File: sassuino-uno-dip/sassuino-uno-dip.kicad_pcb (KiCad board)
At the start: 2 copper layers, 68.6 x 53.3 mm, 30 parts, among them J1 USB_B, J10 OSCPWR_HDR, J2 POWER2_HDR, J3 ICSP_HDR, J4 POWER_HDR, J5 PORTC_HDR, J6 PORTB_HDR, J7 PORTD_HDR, J8 XTAL2_HDR, J9 XTAL1_HDR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

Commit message: Add the actual footprint/model of the pushbutton switch I'm using.
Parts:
- SW1: footprint Button_Switch_THT:SW_PUSH_6mm -> 0SassuinoFP:SW4_1825910-B_TEC
- moved SW1 7.80 mm to (57.8, 146.0)
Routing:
- net /~{RESET}: track 110.8 -> 107.2 mm
- net GND: vias 38 -> 37

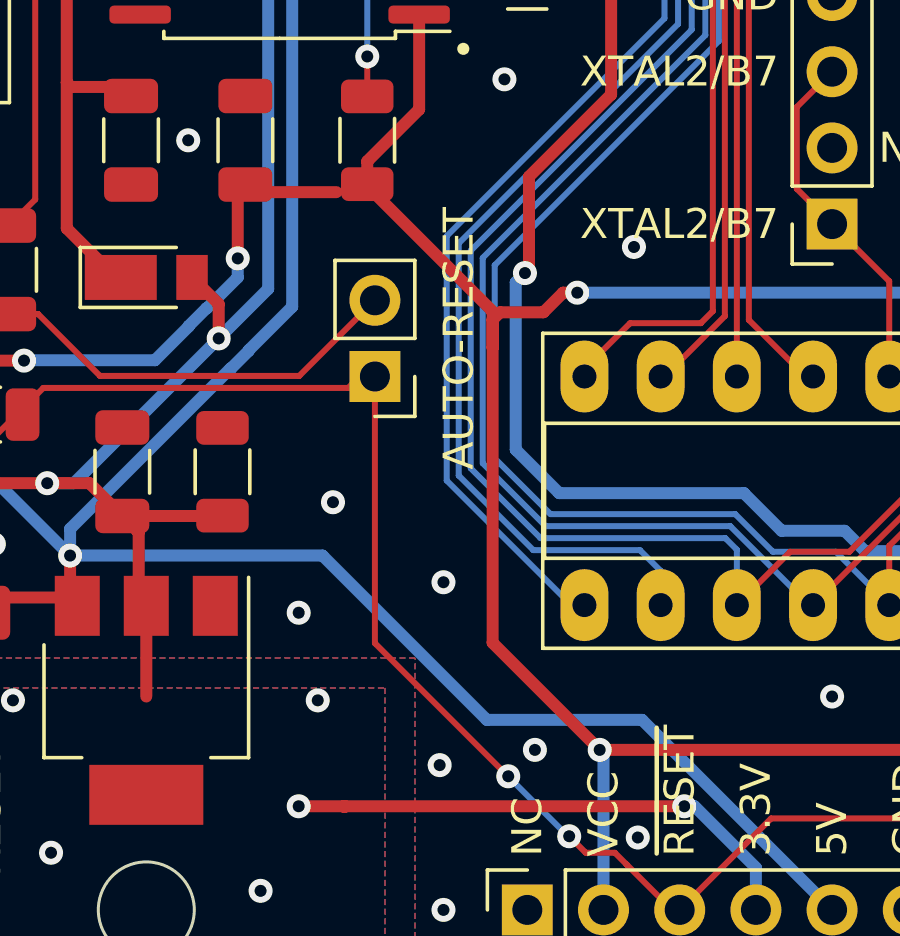
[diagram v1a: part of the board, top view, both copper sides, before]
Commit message: Add a clamp diode to the reset circuit.
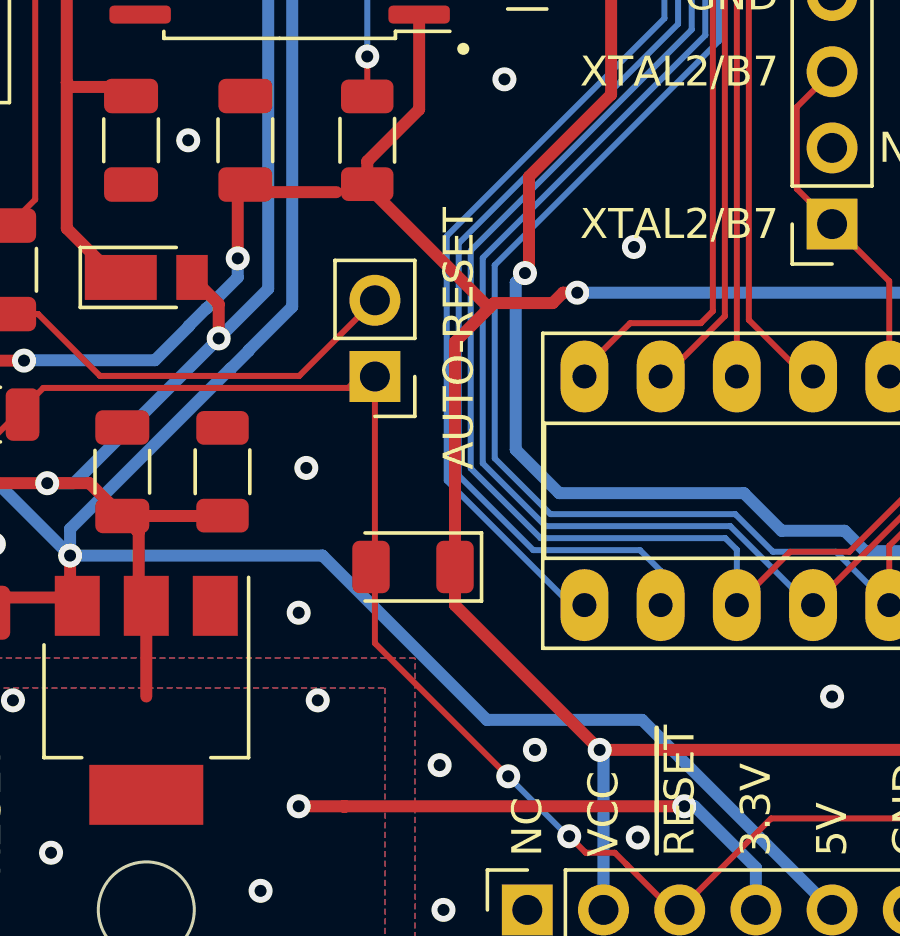
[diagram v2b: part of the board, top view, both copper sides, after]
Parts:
- added D2: TS4148 RAG, Diode_SMD:D_1206_3216Metric, F.Cu at (74.9, 141.0)
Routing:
- net GND: vias 37 -> 36
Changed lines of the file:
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@@
+    )
+  )
+  (footprint "Diode_SMD:D_1206_3216Metric" (layer "F.Cu")
+    (at 74.93 140.97 180)
+    (descr "Diode SMD 1206 (3216 Metric), square (rectangular) end terminal, IPC_7351 nominal, (Body size source: http://www.tortai-tech.com/upload/download/2011102023233369053.pdf), generated with kicad-footprint-generator")
+    (tags "diode")
+    (property "Sheetfile" "sassuino-uno-dip.kicad_sch")
+    (property "Sheetname" "")
+    (attr smd)
+    (fp_text reference "D2" (at 0 -1.82) (layer "F.SilkS") hide
+      (effects (font (size 1 1) (thickness 0.15)))
+    )
+    (fp_text value "TS4148 RAG" (at 0 1.82) (layer "F.Fab")
+      (effects (font (size 1 1) (thickness 0.15)))
+    )
+    (fp_text user "${REFERENCE}" (at 0 0) (layer "F.Fab")
+      (effects (font (size 0.8 0.8) (thickness 0.12)))
+    )
+    (fp_line (start -2.285 -1.135) (end -2.285 1.135) (layer "F.SilkS") (width 0.12))
+    (fp_line (start 1.6 -1.135) (end -2.285 -1.135) (layer "F.SilkS") (width 0.12))
+    (fp_line (start -2.285 1.135) (end 1.6 1.135) (layer "F.SilkS") (width 0.12))
+    (fp_line (start -2.28 -1.12) (end 2.28 -1.12) (layer "F.CrtYd") (width 0.05))
+    (fp_line (start 2.28 -1.12) (end 2.28 1.12) (layer "F.CrtYd") (width 0.05))
+    (fp_line (start 2.28 1.12) (end -2.28 1.12) (layer "F.CrtYd") (width 0.05))
+    (fp_line (start -2.28 1.12) (end -2.28 -1.12) (layer "F.CrtYd") (width 0.05))
+    (fp_line (start -1.6 -0.4) (end -1.6 0.8) (layer "F.Fab") (width 0.1))
+    (fp_line (start 1.6 -0.8) (end -1.2 -0.8) (layer "F.Fab") (width 0.1))
+    (fp_line (start -1.6 0.8) (end 1.6 0.8) (layer "F.Fab") (width 0.1))
+    (fp_line (start 1.6 0.8) (end 1.6 -0.8) (layer "F.Fab") (width 0.1))
+    (fp_line (start -1.2 -0.8) (end -1.6 -0.4) (layer "F.Fab") (width 0.1))
+    (pad "1" smd roundrect (at -1.4 0 180) (size 1.25 1.75) (layers "F.Cu" "F.Paste" "F.Mask") (roundrect_rratio 0.2)
+      (net 29 "VCC") (pinfunction "K") (pintype "passive"))
+    (pad "2" smd roundrect (at 1.4 0 180) (size 1.25 1.75) (layers "F.Cu" "F.Paste" "F.Mask") (roundrect_rratio 0.2)
+      (net 8 "/~{RESET}") (pinfunction "A") (pintype "passive"))
+    (model "${KICAD6_3DMODEL_DIR}/Diode_SMD.3dshapes/D_1206_3216Metric.wrl"
+      (offset (xyz 0 0 0))
+      (scale (xyz 1 1 1))
+      (rotate (xyz 0 0 0))
     )
   )
@@
   (via (at 96.52 112.776) (size 0.8) (drill 0.4) (layers "F.Cu" "B.Cu") (free) (net 2))
   (via (at 85.852 110.8275) (size 0.8) (drill 0.4) (layers "F.Cu" "B.Cu") (free) (net 2))
-  (via (at 72.263 138.811) (size 0.8) (drill 0.4) (layers "F.Cu" "B.Cu") (free) (net 2))
+  (via (at 71.374 137.668) (size 0.8) (drill 0.4) (layers "F.Cu" "B.Cu") (free) (net 2))
   (via (at 102.87 131.318) (size 0.8) (drill 0.4) (layers "F.Cu" "B.Cu") (free) (net 2))
   (via (at 67.437 126.746) (size 0.8) (drill 0.4) (layers "F.Cu" "B.Cu") (free) (net 2))
@@
   (via (at 62.484 107.95) (size 0.8) (drill 0.4) (layers "F.Cu" "B.Cu") (free) (net 2))
   (via (at 58.42 132.588) (size 0.8) (drill 0.4) (layers "F.Cu" "B.Cu") (free) (net 2))
-  (via (at 75.946 141.478) (size 0.8) (drill 0.4) (layers "F.Cu" "B.Cu") (free) (net 2))
   (via (at 110.744 131.826) (size 0.8) (drill 0.4) (layers "F.Cu" "B.Cu") (free) (net 2))
   (via (at 98.679 145.161) (size 0.8) (drill 0.4) (layers "F.Cu" "B.Cu") (free) (net 2))
@@
   (segment (start 86.474352 113.315127) (end 86.088977 113.315127) (width 0.2) (layer "B.Cu") (net 7))
   (segment (start 116.4965 135.89) (end 115.2265 134.62) (width 0.2) (layer "F.Cu") (net 8))
-  (segment (start 78.0961 147.9461) (end 73.66 143.51) (width 0.2) (layer "F.Cu") (net 8))
   (segment (start 86.868 149.352) (end 83.82 152.4) (width 0.2) (layer "F.Cu") (net 8))
-  (segment (start 73.66 143.51) (end 73.66 134.62) (width 0.2) (layer "F.Cu") (net 8))
   (segment (start 72.771 135.001) (end 73.406 134.366) (width 0.2) (layer "F.Cu") (net 8))
   (segment (start 56.642 144.702) (end 56.642 140.967207) (width 0.2) (layer "F.Cu") (net 8))
   (segment (start 82.053 150.887) (end 83.566 152.4) (width 0.2) (layer "F.Cu") (net 8))
   (segment (start 115.2265 134.62) (end 113.665 134.62) (width 0.2) (layer "F.Cu") (net 8))
+  (segment (start 73.66 143.51) (end 73.66 134.62) (width 0.2) (layer "F.Cu") (net 8))
   (segment (start 57.84 145.9) (end 56.642 144.702) (width 0.2) (layer "F.Cu") (net 8))
-  (segment (start 78.105 147.9461) (end 78.0961 147.9461) (width 0.2) (layer "F.Cu") (net 8))
   (segment (start 80.137 149.9451) (end 80.6869 150.495) (width 0.2) (layer "F.Cu") (net 8))
   (segment (start 97.028 149.352) (end 86.868 149.352) (width 0.2) (layer "F.Cu") (net 8))
@@
   (segment (start 57.7596 145.975) (end 53.259599 145.975) (width 0.2) (layer "F.Cu") (net 8))
   (segment (start 80.6869 150.495) (end 81.658207 150.495) (width 0.2) (layer "F.Cu") (net 8))
+  (segment (start 78.105 147.9461) (end 78.0961 147.9461) (width 0.2) (layer "F.Cu") (net 8))
   (segment (start 99.314 147.066) (end 97.028 149.352) (width 0.2) (layer "F.Cu") (net 8))
   (segment (start 82.050207 150.887) (end 82.053 150.887) (width 0.2) (layer "F.Cu") (net 8))
   (segment (start 81.658207 150.495) (end 82.050207 150.887) (width 0.2) (layer "F.Cu") (net 8))
   (segment (start 56.642 140.967207) (end 62.608207 135.001) (width 0.2) (layer "F.Cu") (net 8))
+  (segment (start 78.0961 147.9461) (end 73.66 143.51) (width 0.2) (layer "F.Cu") (net 8))
   (via (at 116.4965 135.89) (size 0.8) (drill 0.4) (layers "F.Cu" "B.Cu") (net 8))
   (via (at 78.105 147.9461) (size 0.8) (drill 0.4) (layers "F.Cu" "B.Cu") (net 8))
@@
   (segment (start 107.95 111.506) (end 106.372 109.928) (width 0.2) (layer "B.Cu") (net 28))
   (segment (start 75.135 125.7175) (end 75.135 122.555) (width 0.4) (layer "F.Cu") (net 29))
-  (segment (start 73.406 128.27) (end 77.5837 132.4477) (width 0.4) (layer "F.Cu") (net 29))
-  (segment (start 77.5837 133.6562) (end 77.5837 143.4967) (width 0.4) (layer "F.Cu") (net 29))
+  (segment (start 73.406 128.2085) (end 73.406 128.27) (width 0.4) (layer "F.Cu") (net 29))
   (segment (start 116.264081 122.682) (end 113.157 122.682) (width 0.4) (layer "F.Cu") (net 29))
+  (segment (start 79.931817 131.826) (end 79.58542 132.172397) (width 0.4) (layer "F.Cu") (net 29))
+  (segment (start 73.406 128.27) (end 77.47 132.334) (width 0.4) (layer "F.Cu") (net 29))
   (segment (start 73.406 128.2085) (end 73.406 127.4465) (width 0.4) (layer "F.Cu") (net 29))
   (segment (start 93.648 146.05) (end 93.648 142.543) (width 0.4) (layer "F.Cu") (net 29))
+  (segment (start 80.405767 131.826) (end 79.931817 131.826) (width 0.4) (layer "F.Cu") (net 29))
   (segment (start 97.91 130.507) (end 97.91 127.071) (width 0.4) (layer "F.Cu") (net 29))
   (segment (start 81.153 147.066) (end 92.632 147.066) (width 0.4) (layer "F.Cu") (net 29))
   (segment (start 92.632 147.066) (end 93.648 146.05) (width 0.4) (layer "F.Cu") (net 29))
-  (segment (start 77.5837 132.7283) (end 77.5837 133.6562) (width 0.4) (layer "F.Cu") (net 29))
   (segment (start 112.522 123.317) (end 112.522 126.161704) (width 0.4) (layer "F.Cu") (net 29))
-  (segment (start 77.5837 143.4967) (end 81.153 147.066) (width 0.4) (layer "F.Cu") (net 29))
   (segment (start 97.91 131.826) (end 97.91 130.507) (width 0.4) (layer "F.Cu") (net 29))
   (segment (start 57.7195 137.16) (end 53.93 137.16) (width 0.4) (layer "F.Cu") (net 29))
+  (segment (start 79.58542 132.172397) (end 77.631603 132.172397) (width 0.4) (layer "F.Cu") (net 29))
   (segment (start 97.91 130.507) (end 97.91 134.105) (width 0.4) (layer "F.Cu") (net 29))
-  (segment (start 79.931817 131.826) (end 79.277817 132.48) (width 0.4) (layer "F.Cu") (net 29))
   (segment (start 69.596 128.475) (end 72.3775 128.475) (width 0.4) (layer "F.Cu") (net 29))
-  (segment (start 77.5837 132.4477) (end 77.5837 133.6562) (width 0.4) (layer "F.Cu") (net 29))
   (segment (start 116.84 123.257919) (end 116.264081 122.682) (width 0.4) (layer "F.Cu") (net 29))
   (segment (start 69.342 128.221) (end 69.596 128.475) (width 0.4) (layer "F.Cu") (net 29))
   (segment (start 112.522 126.161704) (end 109.22 129.463704) (width 0.4) (layer "F.Cu") (net 29))
+  (segment (start 77.47 132.334) (end 76.33 133.474) (width 0.4) (layer "F.Cu") (net 29))
   (segment (start 69.088 130.683) (end 69.088 128.729) (width 0.4) (layer "F.Cu") (net 29))
-  (segment (start 80.405767 131.826) (end 79.931817 131.826) (width 0.4) (layer "F.Cu") (net 29))
   (segment (start 61.963481 134.090568) (end 60.788932 134.090568) (width 0.4) (layer "F.Cu") (net 29))
   (segment (start 58.9895 135.89) (end 57.7195 137.16) (width 0.4) (layer "F.Cu") (net 29))
-  (segment (start 79.277817 132.48) (end 77.832 132.48) (width 0.4) (layer "F.Cu") (net 29))
   (segment (start 113.157 122.682) (end 112.522 123.317) (width 0.4) (layer "F.Cu") (net 29))
-  (segment (start 73.406 128.2085) (end 73.406 128.27) (width 0.4) (layer "F.Cu") (net 29))
-  (segment (start 77.832 132.48) (end 77.5837 132.7283) (width 0.4) (layer "F.Cu") (net 29))
   (segment (start 60.788932 134.090568) (end 58.9895 135.89) (width 0.4) (layer "F.Cu") (net 29))
+  (segment (start 77.631603 132.172397) (end 77.47 132.334) (width 0.4) (layer "F.Cu") (net 29))
+  (segment (start 76.33 142.243) (end 81.153 147.066) (width 0.4) (layer "F.Cu") (net 29))
+  (segment (start 76.33 133.474) (end 76.33 142.243) (width 0.4) (layer "F.Cu") (net 29))
   (segment (start 116.84 124.46) (end 116.84 123.257919) (width 0.4) (layer "F.Cu") (net 29))
   (segment (start 73.406 127.4465) (end 75.135 125.7175) (width 0.4) (layer "F.Cu") (net 29))
